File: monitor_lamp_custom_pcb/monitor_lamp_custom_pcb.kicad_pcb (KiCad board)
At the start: 2 copper layers, 50 x 35 mm, 26 parts, among them IC1 HUSB238, J1 USB_C_Receptacle_PowerOnly_6P, J2 VEML7700_Connection, J3 LD2410C_Connection, J4 Conn_01x02, Q1 AO3401A, Q2 AO3401A, Q3 AO3400A, U1 TPS5430DDA, U3 ESP32-C3_SUPERMINI_TH

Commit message: Placed connection pad
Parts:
- added J5: Conn_01x01, Connector_Wire:SolderWirePad_1x01_SMD_2x4mm, F.Cu at (144.1, 82.6)
- added J7: Conn_01x01, Connector_Wire:SolderWirePad_1x01_SMD_2x4mm, F.Cu at (144.1, 79.0)
- added J8: Conn_01x01, Connector_Wire:SolderWirePad_1x01_SMD_2x4mm, F.Cu at (135.0, 59.5)
- added J9: Conn_01x01, Connector_Wire:SolderWirePad_1x01_SMD_2x4mm, F.Cu at (135.0, 56.0)
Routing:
- net /ESP32_Sensors_Mosfet/5V_Protected: track 24.2 -> 41.5 mm
- net GND: track 40.2 -> 48.0 mm, vias 28 -> 38
- net /+5V: track 23.2 -> 21.6 mm
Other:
- board text added: "+5V"
- board text added: "GND"

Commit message: almost done
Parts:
- IC1: footprint Custom_Components:SON50P300X300X80-11N-D -> Custom_Components:DFN-10L
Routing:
- net GND: vias 38 -> 39
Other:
- board text added: "By Giakk"
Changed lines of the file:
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@@
 			(plot_on_all_layers_selection 0x00000000_00000000_00000000_00000000)
 			(disableapertmacros no)
-			(usegerberextensions no)
+			(usegerberextensions yes)
 			(usegerberattributes yes)
 			(usegerberadvancedattributes yes)
-			(creategerberjobfile yes)
+			(creategerberjobfile no)
 			(dashed_line_dash_ratio 12)
 			(dashed_line_gap_ratio 3)
@@
 			(outputformat 1)
 			(mirror no)
-			(drillshape 1)
+			(drillshape 0)
 			(scaleselection 1)
-			(outputdirectory "")
+			(outputdirectory "gerber/")
 		)
 	)
-	(footprint "Custom_Components:SON50P300X300X80-11N-D"
+	(footprint "Custom_Components:DFN-10L"
 		(layer "F.Cu")
 		(at 120.225 62.5 180)
@@
 		(tags "Integrated Circuit")
 		(property "Reference" "IC1"
-			(at -2.875 1.3 90)
+			(at 0 0 180)
 			(layer "F.SilkS")
 			(effects
 				(font
-					(size 1 1)
-					(thickness 0.15)
+					(size 1.27 1.27)
+					(thickness 0.254)
 				)
 			)
 		)
 		(property "Value" "HUSB238"
-			(at 0 0 0)
+			(at 0 0 180)
 			(layer "F.SilkS")
 			(hide yes)
@@
 		)
 		(property "Datasheet" "https://en.hynetek.com/uploadfiles/site/219/news/4459b599-ce6b-4d92-83cc-13212cca0672.pdf"
-			(at 0 0 0)
+			(at 0 0 180)
 			(layer "F.Fab")
 			(hide yes)
@@
 		)
 		(property "Description" "USB Type-C Power Delivery Sink"
-			(at 0 0 0)
+			(at 0 0 180)
 			(layer "F.Fab")
 			(hide yes)
@@
 		)
 		(fp_text user "${REFERENCE}"
-			(at 0 0 0)
+			(at 0 0 180)
 			(layer "F.Fab")
 			(effects
@@
 		)
 	)
+	(gr_text "By Giakk"
+		(at 117.9 86.3 0)
+		(layer "F.SilkS")
+		(effects
+			(font
+				(size 1 1)
+				(thickness 0.2)
+				(bold yes)
+			)
+			(justify left bottom)
+		)
+	)
 	(gr_text "ESP32-C3\nSupermini"
 		(at 152 72.8 90)
@@
 		(size 0.6)
 		(drill 0.3)
+		(layers "F.Cu" "B.Cu")
+		(free yes)
+		(net "GND")
+	)
+	(via
+		(at 130 54.7)
+		(size 0.6)
+		(drill 0.3)

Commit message: Added some drawing to the board and recreated fabbrication file
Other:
- board text added: "By Giakk Light your desk..."
- board text removed: "By Giakk"
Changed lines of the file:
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@@
 		(tags "Integrated Circuit")
 		(property "Reference" "IC1"
-			(at 0 0 180)
+			(at -2.125 1.8 180)
 			(layer "F.SilkS")
 			(effects
 				(font
-					(size 1.27 1.27)
-					(thickness 0.254)
+					(size 0.6 0.6)
+					(thickness 0.1)
+					(bold yes)
 				)
 			)
@@
 			)
 		)
-		(attr smd)
+		(attr smd exclude_from_bom)
 		(duplicate_pad_numbers_are_jumpers no)
 		(fp_line
@@
 			)
 		)
-		(attr through_hole)
+		(attr through_hole exclude_from_bom)
 		(duplicate_pad_numbers_are_jumpers no)
 		(fp_line
@@
 			)
 		)
-		(attr smd)
+		(attr smd exclude_from_bom)
 		(duplicate_pad_numbers_are_jumpers no)
 		(fp_line
@@
 			)
 		)
-		(attr through_hole)
+		(attr through_hole exclude_from_bom)
 		(duplicate_pad_numbers_are_jumpers no)
 		(fp_line
@@
 			)
 		)
-		(attr smd)
+		(attr smd exclude_from_bom)
 		(duplicate_pad_numbers_are_jumpers no)
 		(fp_line
@@
 			)
 		)
-		(property "LCSC" "C2894893"
+		(property "LCSC" "C283540"
 			(at 0 0 180)
 			(unlocked yes)
@@
 			)
 		)
-		(attr smd)
+		(attr smd exclude_from_bom)
 		(duplicate_pad_numbers_are_jumpers no)
 		(fp_line
@@
 		)
 	)
+	(gr_circle
+		(center 161.23 75.225)
+		(end 161.35 75.225)
+		(stroke
+			(width 0.1)
+			(type solid)
+		)
+		(fill yes)
+		(layer "F.SilkS")
+	)
+	(gr_line
+		(start 161.23 75.225)
+		(end 162.2 77.025)
+		(stroke
+			(width 0.07)
+			(type solid)
+		)
+		(layer "F.SilkS")
+	)
+	(gr_circle
+		(center 162.15 73.525)
+		(end 162.27 73.525)
+		(stroke
+			(width 0.1)
+			(type solid)
+		)
+		(fill yes)
+		(layer "F.SilkS")
+	)
+	(gr_line
+		(start 162.15 73.525)
+		(end 162.35 74.775)
+		(stroke
+			(width 0.07)
+			(type solid)
+		)
+		(layer "F.SilkS")
+	)
+	(gr_circle
+		(center 162.2 77.025)
+		(end 162.32 77.025)
+		(stroke
+			(width 0.1)
+			(type solid)
+		)
+		(fill yes)
+		(layer "F.SilkS")
+	)
+	(gr_line
+		(start 162.2 77.025)
+		(end 163.25 76.225)
+		(stroke
+			(width 0.07)
+			(type solid)
+		)
+		(layer "F.SilkS")
+	)
+	(gr_line
+		(start 162.35 74.775)
+		(end 161.23 75.225)
+		(stroke
+			(width 0.07)
+			(type solid)
+		)
+		(layer "F.SilkS")
+	)
+	(gr_circle
+		(center 162.35 74.775)
+		(end 162.47 74.775)
+		(stroke
+			(width 0.1)
+			(type solid)
+		)
+		(fill yes)
+		(layer "F.SilkS")
+	)
+	(gr_line
+		(start 162.4 72.225)
+		(end 162.15 73.525)
+		(stroke
+			(width 0.07)
+			(type solid)
+		)
+		(layer "F.SilkS")
+	)
+	(gr_circle
+		(center 162.4 72.225)
+		(end 162.52 72.225)
+		(stroke
+			(width 0.1)
+			(type solid)
+		)
+		(fill yes)
+		(layer "F.SilkS")
+	)
+	(gr_line
+		(start 162.9 71.175)
+		(end 162.4 72.225)
+		(stroke
+			(width 0.07)
+			(type solid)
+		)
+		(layer "F.SilkS")
+	)
+	(gr_circle
+		(center 162.9 71.175)
+		(end 163.02 71.175)
+		(stroke
+			(width 0.1)
+			(type solid)
+		)
+		(fill yes)
+		(layer "F.SilkS")
+	)
+	(gr_line
+		(start 163 70.9)
+		(end 163.05 70.85)
+		(stroke
+			(width 0.1)
+			(type default)
+		)
+		(layer "F.SilkS")
+	)
+	(gr_line
+		(start 163.1 71.45)
+		(end 163.8 71.9)
+		(stroke
+			(width 0.1)
+			(type default)
+		)
+		(layer "F.SilkS")
+	)
+	(gr_line
+		(start 163.25 76.225)
+		(end 162.35 74.775)
+		(stroke
+			(width 0.07)
+			(type solid)
+		)
+		(layer "F.SilkS")
+	)
+	(gr_circle
+		(center 163.25 76.225)
+		(end 163.37 76.225)
+		(stroke
+			(width 0.1)
+			(type solid)
+		)
+		(fill yes)
+		(layer "F.SilkS")
+	)
+	(gr_line
+		(start 163.2868 70.90288)
+		(end 163.1368 71.00288)
+		(stroke
+			(width 0.1)
+			(type default)
+		)
+		(layer "F.SilkS")
+	)
+	(gr_line
+		(start 163.5118 71.10288)
+		(end 163.1618 71.15288)
+		(stroke
+			(width 0.1)
+			(type default)
+		)
+		(layer "F.SilkS")
+	)
+	(gr_line
+		(start 163.7118 71.50288)
+		(end 163.1618 71.30288)
+		(stroke
+			(width 0.1)
+			(type default)
+		)
+		(layer "F.SilkS")
+	)
 	(gr_rect
 		(start 115.88 53.24)
@@
 		)
 	)
-	(gr_text "By Giakk"
+	(gr_text "By Giakk	Light your desk..."
 		(at 117.9 86.3 0)
 		(layer "F.SilkS")
@@
 		)
 	)
+	(group ""
+		(members "05aedfff-e97b-4af1-ac91-2099e680c3b0" "0ab984d1-31dc-498e-947c-a3cf54af8d4e"
+			"1e842ff7-0704-483a-bdf0-35a7c5ff4ca3" "39923241-027e-434d-8c9e-acbf4e878f3b"
+			"3d330d68-f890-4f1f-9309-ef6ee1efe8bb" "5a7cc059-1e61-459c-ab21-35e068d2dba2"
+			"76bbe0b0-c543-4286-993c-8636d6b24b36" "7cf4f424-6374-4bfc-9a63-3a5cd7f664fc"
+			"9d75d27c-77da-476b-9158-4c0c6462ae22" "ad2be0f2-08c4-42b8-8c22-5410f6a68a38"
+			"b3d50250-b40d-4ae1-8f4e-f532e3e8b64f" "c3811027-40aa-4d7d-b2f0-2b4e183bf487"
+			"e8ac955f-552f-49e8-b5b9-c8aeb40107f4" "ee9fe9af-e5ce-47f6-8e33-4e6c48ea62ac"
+		)
+	)
+	(group ""
+		(members "0c9e52b3-1f4f-4214-8ed9-7e12389ce698" "29f46efc-b4b0-4c42-ae73-9148a8f543ec"
+			"5dac70f1-7836-4da1-aeef-73a9adfe83fa" "73a56b0d-f821-40d1-8683-cdf115a02169"
+			"b0672947-a073-43da-83be-d3ef559a791d" "d4b2ada7-0357-4d55-8d84-c4907cc379bf"
+		)
+	)

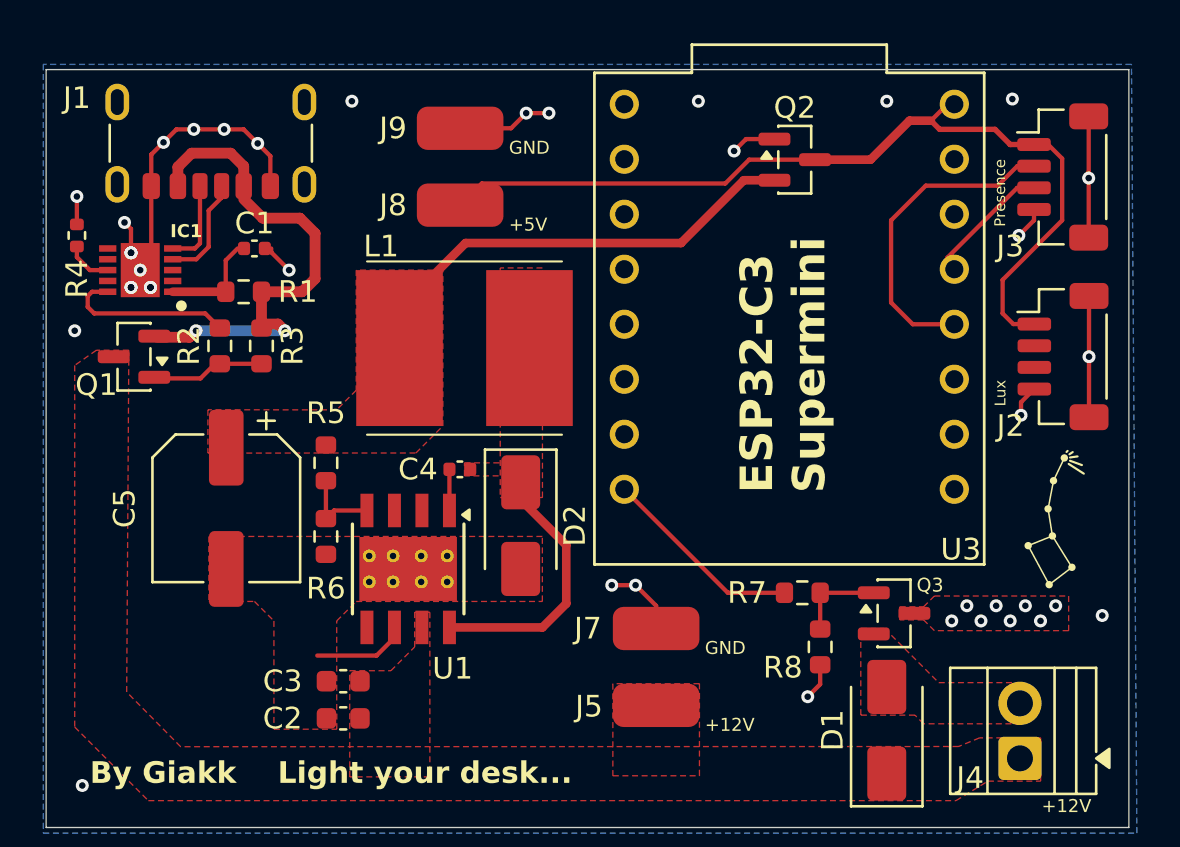
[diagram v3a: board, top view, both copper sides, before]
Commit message: Changed connector to JST PH 2.0mm
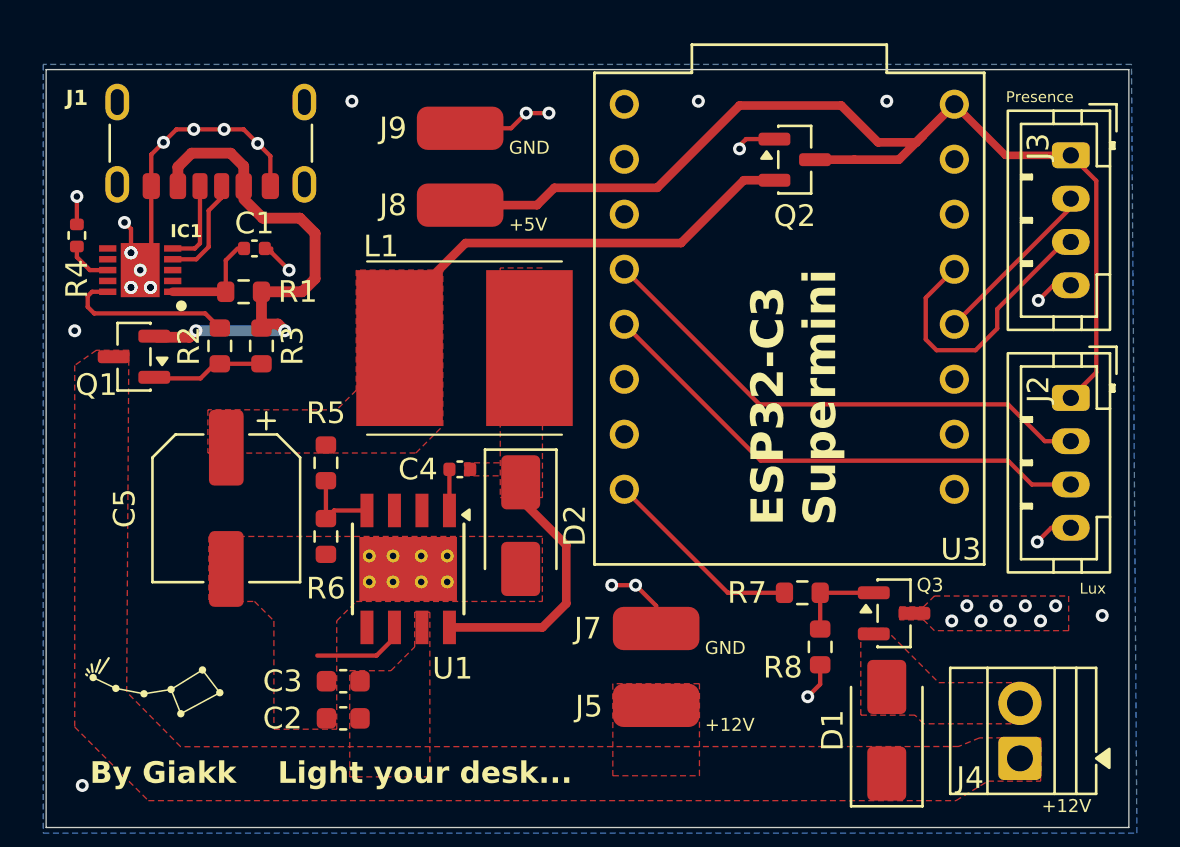
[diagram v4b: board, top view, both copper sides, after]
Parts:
- J2, J3: footprint Connector_JST:JST_SH_BM04B-SRSS-TB_1x04-1MP_P1.00mm_Vertical -> Connector_JST:JST_PH_B4B-PH-K_1x04_P2.00mm_Vertical
- moved J2 1.94 mm to (163.2, 68.4)
- moved J3 1.07 mm to (163.2, 57.2)
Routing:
- net /ESP32_Sensors_Mosfet/SDA: track 0.00 -> 23.9 mm
- net /ESP32_Sensors_Mosfet/SCL: track 0.00 -> 23.7 mm
- net GND: track 48.0 -> 37.3 mm, vias 39 -> 36
- net /ESP32_Sensors_Mosfet/5V_Protected: track 41.5 -> 50.7 mm
- net Net-(J3-Pin_3): track 6.00 -> 13.3 mm
- net Net-(J3-Pin_2): track 14.8 -> 8.03 mm

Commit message: Definitive version - Ordered on JLCPCB
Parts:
- added H1: MountingHole, MountingHole:MountingHole_2.2mm_M2, F.Cu at (123.0, 81.3)
- added H2: MountingHole, MountingHole:MountingHole_2.2mm_M2, F.Cu at (152.8, 64.8)

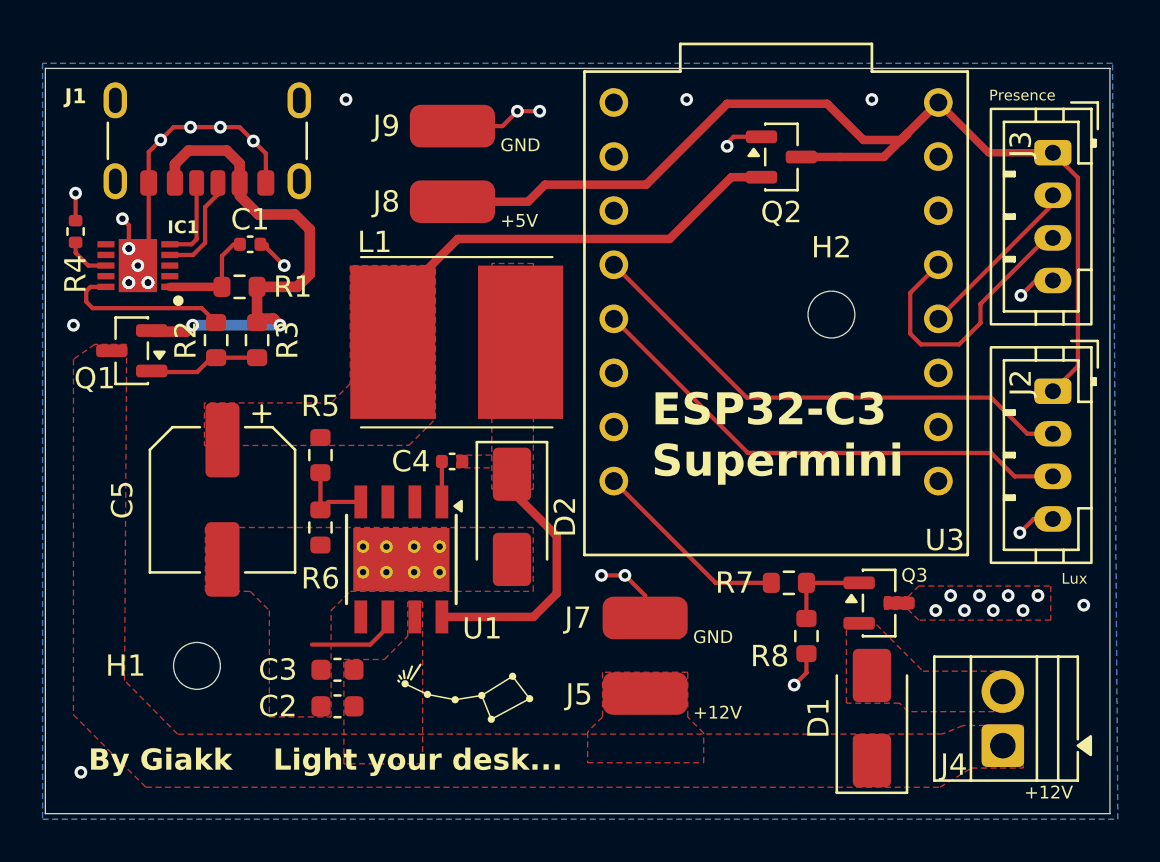
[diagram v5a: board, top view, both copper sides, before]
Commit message: Added ISET resistor for solving 12V issue on previous release
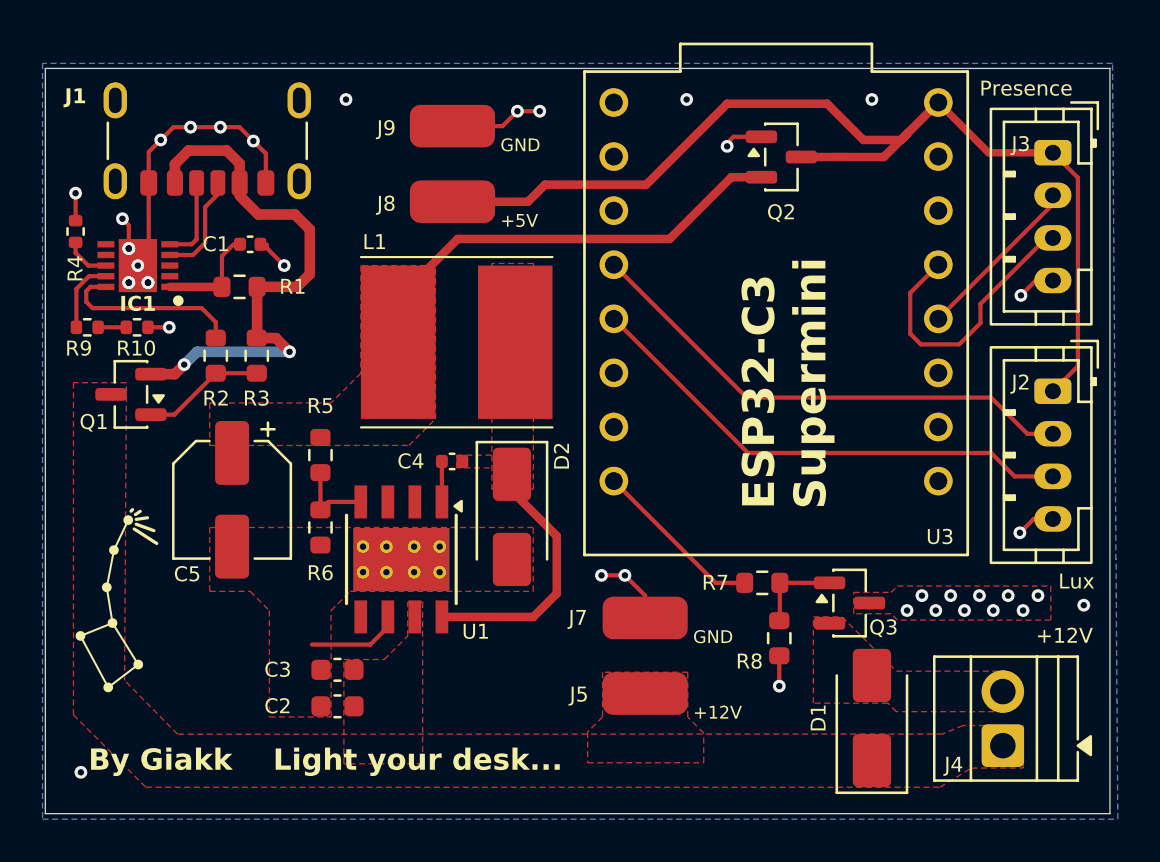
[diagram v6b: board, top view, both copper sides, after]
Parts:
- removed H1, H2: MountingHole, MountingHole:MountingHole_2.2mm_M2
- added R10: 510, Resistor_SMD:R_0402_1005Metric, F.Cu at (120.2, 65.4)
- added R9: 10k, Resistor_SMD:R_0402_1005Metric, F.Cu at (117.8, 65.4)
- C5: footprint Capacitor_SMD:CP_Elec_6.3x5.4 -> Capacitor_SMD:CP_Elec_5x5.4
- moved Q1 2.05 mm to (119.9, 68.5)
- moved Q3 1.39 mm to (153.7, 78.3)
- moved R8 1.28 mm to (150.3, 80.0)
- moved R7 1.25 mm to (149.6, 77.4)
- moved R2 0.73 mm to (123.9, 66.7)
- moved R3 0.73 mm to (125.8, 66.7)
- moved C5 0.45 mm to (124.7, 73.5)
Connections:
- IC1 pad 9: unconnected-(IC1-ISET-Pad9) -> Net-(IC1-ISET)
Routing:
- net Net-(IC1-ISET): track 0.00 -> 3.44 mm
- net Net-(Q1-S): track 23.4 -> 25.9 mm
- net Net-(R10-Pad1): track 0.00 -> 1.32 mm
- net PWM_Control: track 9.37 -> 8.12 mm
- net Net-(IC1-GATE): track 8.01 -> 8.74 mm
- net GND: track 37.3 -> 38.0 mm, vias 36 -> 38
- net Net-(Q1-G): track 5.10 -> 5.78 mm
